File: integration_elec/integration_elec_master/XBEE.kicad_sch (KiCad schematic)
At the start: 12 parts, among them Q1 Q_NMOS_GSD, U2 XBEE_PRO_900HP

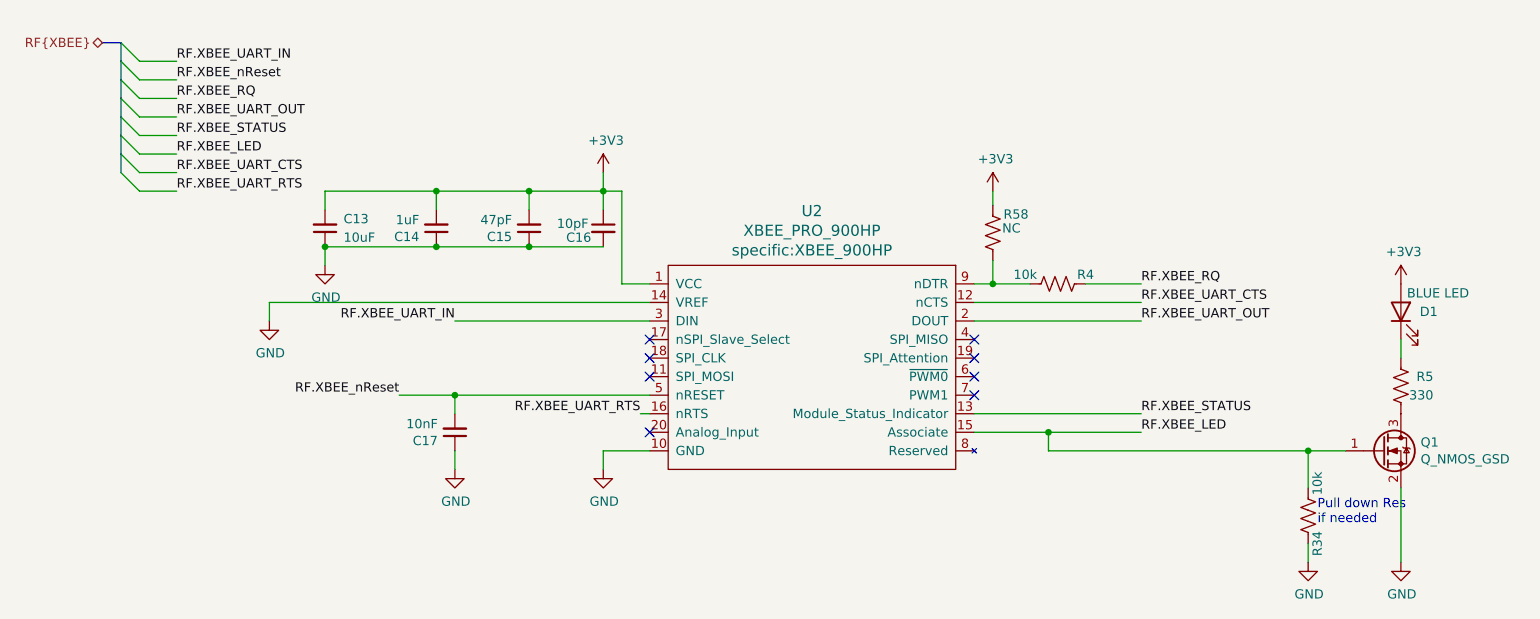
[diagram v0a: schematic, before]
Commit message: Added footprint, symbol, 3D model for joystick. Added schematic for Joystick and comments
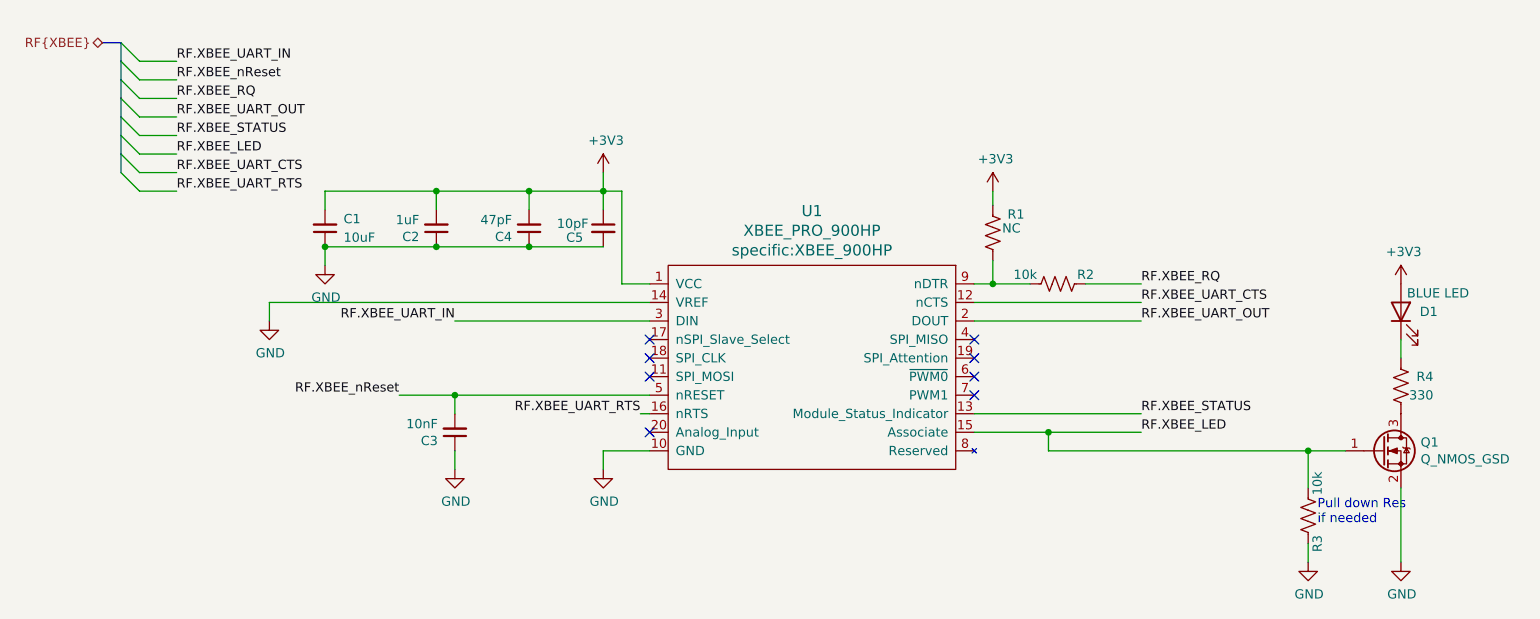
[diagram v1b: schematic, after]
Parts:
- renumbered C13 to C1, C14 to C2, C17 to C3, C15 to C4, C16 to C5, R58 to R1, R4 to R2, R34 to R3, R5 to R4, U2 to U1
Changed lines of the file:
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@@
 		(on_board yes)
 		(dnp no)
-		(property "Reference" "U2"
+		(property "Reference" "U1"
 			(at 147.955 76.3778 0)
 			(effects
@@
 			(project "integration_elec_master"
 				(path "/7d904e0d-c2b1-4329-81a9-fc34d181a4fe/53810e40-2580-4e56-a6c6-cf1eae4bc5f8"
-					(reference "U2")
+					(reference "U1")
 					(unit 1)
 				)
@@
 		(on_board yes)
 		(dnp no)
-		(property "Reference" "#PWR011"
+		(property "Reference" "#PWR04"
 			(at 119.38 74.93 0)
 			(effects
@@
 			(project "integration_elec_master"
 				(path "/7d904e0d-c2b1-4329-81a9-fc34d181a4fe/53810e40-2580-4e56-a6c6-cf1eae4bc5f8"
-					(reference "#PWR011")
+					(reference "#PWR04")
 					(unit 1)
 				)
@@
 		(on_board yes)
 		(dnp no)
-		(property "Reference" "#PWR017"
+		(property "Reference" "#PWR05"
 			(at 119.38 118.11 0)
 			(effects
@@
 			(project "integration_elec_master"
 				(path "/7d904e0d-c2b1-4329-81a9-fc34d181a4fe/53810e40-2580-4e56-a6c6-cf1eae4bc5f8"
-					(reference "#PWR017")
+					(reference "#PWR05")
 					(unit 1)
 				)
@@
 		(on_board yes)
 		(dnp no)
-		(property "Reference" "#PWR015"
+		(property "Reference" "#PWR01"
 			(at 73.66 97.79 0)
 			(effects
@@
 			(project "integration_elec_master"
 				(path "/7d904e0d-c2b1-4329-81a9-fc34d181a4fe/53810e40-2580-4e56-a6c6-cf1eae4bc5f8"
-					(reference "#PWR015")
+					(reference "#PWR01")
 					(unit 1)
 				)
@@
 		(on_board yes)
 		(dnp no)
-		(property "Reference" "C17"
+		(property "Reference" "C3"
 			(at 96.7232 107.8484 0)
 			(effects
@@
 			(project "integration_elec_master"
 				(path "/7d904e0d-c2b1-4329-81a9-fc34d181a4fe/53810e40-2580-4e56-a6c6-cf1eae4bc5f8"
-					(reference "C17")
+					(reference "C3")
 					(unit 1)
 				)
@@
 		(on_board yes)
 		(dnp no)
-		(property "Reference" "#PWR016"
+		(property "Reference" "#PWR03"
 			(at 99.06 118.11 0)
 			(effects
@@
 			(project "integration_elec_master"
 				(path "/7d904e0d-c2b1-4329-81a9-fc34d181a4fe/53810e40-2580-4e56-a6c6-cf1eae4bc5f8"
-					(reference "#PWR016")
+					(reference "#PWR03")
 					(unit 1)
 				)
@@
 		(on_board yes)
 		(dnp no)
-		(property "Reference" "#PWR012"
+		(property "Reference" "#PWR06"
 			(at 172.72 77.47 0)
 			(effects
@@
 			(project "integration_elec_master"
 				(path "/7d904e0d-c2b1-4329-81a9-fc34d181a4fe/53810e40-2580-4e56-a6c6-cf1eae4bc5f8"
-					(reference "#PWR012")
+					(reference "#PWR06")
 					(unit 1)
 				)
@@
 		(on_board yes)
 		(dnp no)
-		(property "Reference" "R4"
+		(property "Reference" "R2"
 			(at 185.42 85.09 90)
 			(effects
@@
 			(project "integration_elec_master"
 				(path "/7d904e0d-c2b1-4329-81a9-fc34d181a4fe/53810e40-2580-4e56-a6c6-cf1eae4bc5f8"
-					(reference "R4")
+					(reference "R2")
 					(unit 1)
 				)
@@
 		(on_board yes)
 		(dnp no)
-		(property "Reference" "#PWR018"
+		(property "Reference" "#PWR09"
 			(at 228.6 130.81 0)
 			(effects
@@
 			(project "integration_elec_master"
 				(path "/7d904e0d-c2b1-4329-81a9-fc34d181a4fe/53810e40-2580-4e56-a6c6-cf1eae4bc5f8"
-					(reference "#PWR018")
+					(reference "#PWR09")
 					(unit 1)
 				)
@@
 		(on_board yes)
 		(dnp no)
-		(property "Reference" "R5"
+		(property "Reference" "R4"
 			(at 233.045 99.06 0)
 			(effects
@@
 			(project "integration_elec_master"
 				(path "/7d904e0d-c2b1-4329-81a9-fc34d181a4fe/53810e40-2580-4e56-a6c6-cf1eae4bc5f8"
-					(reference "R5")
+					(reference "R4")
 					(unit 1)
 				)
@@
 		(on_board yes)
 		(dnp no)
-		(property "Reference" "#PWR014"
+		(property "Reference" "#PWR08"
 			(at 228.6 90.17 0)
 			(effects
@@
 			(project "integration_elec_master"
 				(path "/7d904e0d-c2b1-4329-81a9-fc34d181a4fe/53810e40-2580-4e56-a6c6-cf1eae4bc5f8"
-					(reference "#PWR014")
+					(reference "#PWR08")
 					(unit 1)
 				)
@@
 		(on_board yes)
 		(dnp no)
-		(property "Reference" "R34"
+		(property "Reference" "R3"
 			(at 217.17 121.92 90)
 			(effects
@@
 			(project "integration_elec_master"
 				(path "/7d904e0d-c2b1-4329-81a9-fc34d181a4fe/53810e40-2580-4e56-a6c6-cf1eae4bc5f8"
-					(reference "R34")
+					(reference "R3")
 					(unit 1)
 				)
@@
 		(on_board yes)
 		(dnp no)
-		(property "Reference" "#PWR0101"
+		(property "Reference" "#PWR07"
 			(at 215.9 130.81 0)
 			(effects
@@
 			(project "integration_elec_master"
 				(path "/7d904e0d-c2b1-4329-81a9-fc34d181a4fe/53810e40-2580-4e56-a6c6-cf1eae4bc5f8"
-					(reference "#PWR0101")
+					(reference "#PWR07")
 					(unit 1)
 				)
@@
 		(on_board yes)
 		(dnp no)
-		(property "Reference" "R58"
+		(property "Reference" "R1"
 			(at 175.895 76.835 0)
 			(effects
@@
 			(project "integration_elec_master"
 				(path "/7d904e0d-c2b1-4329-81a9-fc34d181a4fe/53810e40-2580-4e56-a6c6-cf1eae4bc5f8"
-					(reference "R58")
+					(reference "R1")
 					(unit 1)
 				)
@@
 		(on_board yes)
 		(dnp no)
-		(property "Reference" "C16"
+		(property "Reference" "C5"
 			(at 114.3 80.01 0)
 			(effects
@@
 			(project "integration_elec_master"
 				(path "/7d904e0d-c2b1-4329-81a9-fc34d181a4fe/53810e40-2580-4e56-a6c6-cf1eae4bc5f8"
-					(reference "C16")
+					(reference "C5")
 					(unit 1)
 				)
@@
 		(on_board yes)
 		(dnp no)
-		(property "Reference" "#PWR013"
+		(property "Reference" "#PWR02"
 			(at 81.28 90.17 0)
 			(effects
@@
 			(project "integration_elec_master"
 				(path "/7d904e0d-c2b1-4329-81a9-fc34d181a4fe/53810e40-2580-4e56-a6c6-cf1eae4bc5f8"
-					(reference "#PWR013")
+					(reference "#PWR02")
 					(unit 1)
 				)
@@
 		(on_board yes)
 		(dnp no)
-		(property "Reference" "C15"
+		(property "Reference" "C4"
 			(at 106.8832 79.9084 0)
 			(effects
@@
 			(project "integration_elec_master"
 				(path "/7d904e0d-c2b1-4329-81a9-fc34d181a4fe/53810e40-2580-4e56-a6c6-cf1eae4bc5f8"
-					(reference "C15")
+					(reference "C4")
 					(unit 1)
 				)
@@
 		(dnp no)
 		(fields_autoplaced yes)
-		(property "Reference" "C13"
+		(property "Reference" "C1"
 			(at 83.82 77.4636 0)
 			(effects
@@
 			(project "integration_elec_master"
 				(path "/7d904e0d-c2b1-4329-81a9-fc34d181a4fe/53810e40-2580-4e56-a6c6-cf1eae4bc5f8"
-					(reference "C13")
+					(reference "C1")
 					(unit 1)
 				)
@@
 		(on_board yes)
 		(dnp no)
-		(property "Reference" "C14"
+		(property "Reference" "C2"
 			(at 94.1832 79.9084 0)
 			(effects
@@
 			(project "integration_elec_master"
 				(path "/7d904e0d-c2b1-4329-81a9-fc34d181a4fe/53810e40-2580-4e56-a6c6-cf1eae4bc5f8"
-					(reference "C14")
-					(unit 1)
-				)
+					(reference "C2")
+					(unit 1)
+				)

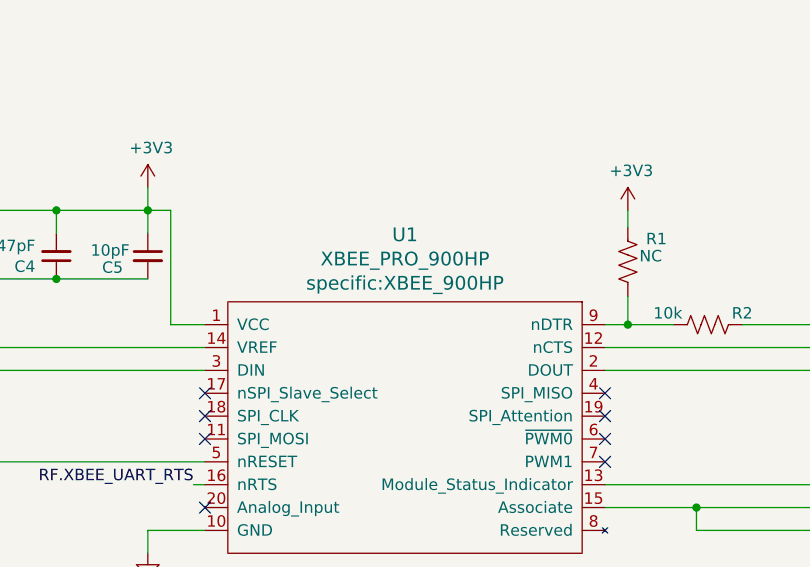
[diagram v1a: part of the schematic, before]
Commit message: Added plein de footprint
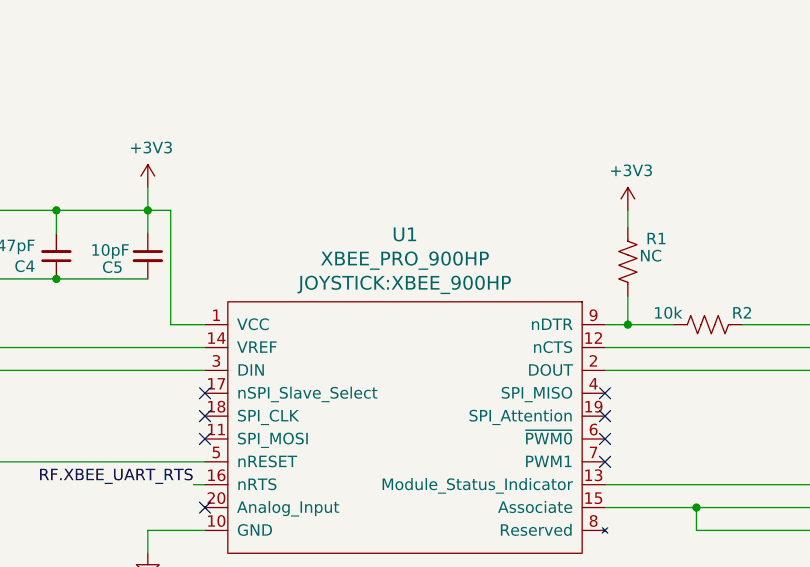
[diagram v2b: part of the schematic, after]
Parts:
- U1: footprint specific:XBEE_900HP -> JOYSTICK:XBEE_900HP
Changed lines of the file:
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@@
 			)
 		)
-		(property "Footprint" "specific:XBEE_900HP"
+		(property "Footprint" "JOYSTICK:XBEE_900HP"
 			(at 147.955 81.7626 0)
 			(effects

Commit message: KAH - added the part # for some pieces. MISSING R NC and USB-C conn
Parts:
- U1: now left out of the parts list
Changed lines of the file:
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@@
 		(unit 1)
 		(exclude_from_sim no)
-		(in_bom yes)
+		(in_bom no)
 		(on_board yes)
 		(dnp no)
